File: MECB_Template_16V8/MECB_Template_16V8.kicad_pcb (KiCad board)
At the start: 2 copper layers, 99.8 x 99.8 mm, 7 parts, among them J1 MECB_64AC, U1 ATF16V8

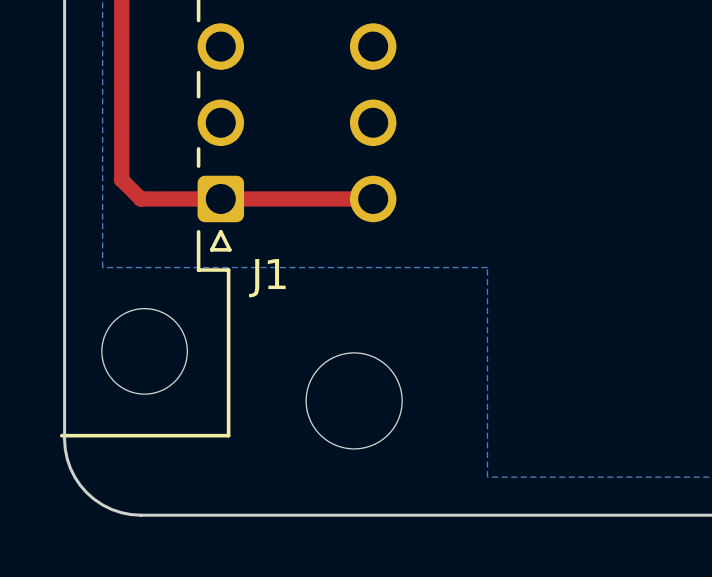
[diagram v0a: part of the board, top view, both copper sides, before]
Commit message: MECB_Template_16V8 - Update to KiCAD v10.0.  Add missing MECB footprint library folder.
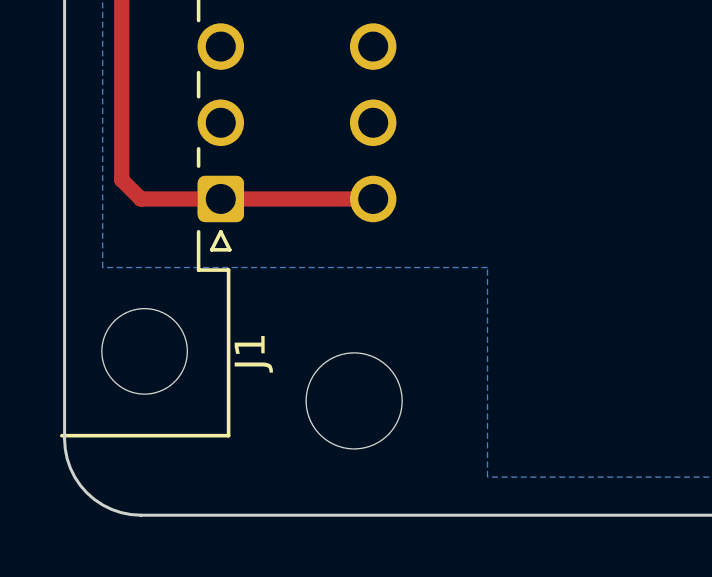
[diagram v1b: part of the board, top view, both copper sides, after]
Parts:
- J1: footprint MyCustomFootprintLibrary:DIN41612_C_2x32_C64AC_Male_Horizontal_THT -> MECB:DIN41612_C_2x32_C64AC_Male_Horizontal_THT
- U1: footprint MyCustomFootprintLibrary:DIP-20_W7.62mm_Socket_LongPads_ZIF_friendly -> MECB:DIP-20_W7.62mm_Socket_LongPads_ZIF_friendly
